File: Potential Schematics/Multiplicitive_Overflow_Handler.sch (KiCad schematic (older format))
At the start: 7 parts, among them SW1 SW_Push, U25 74LS04, U26 74LS08, U28 74LS08

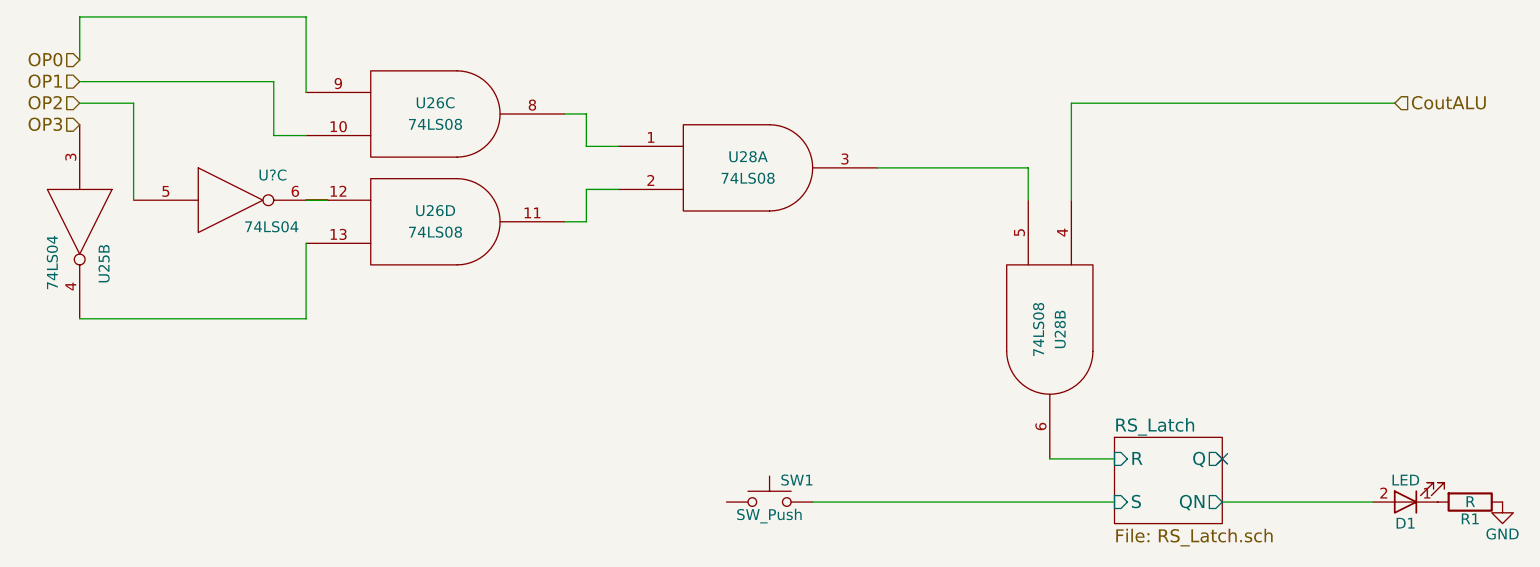
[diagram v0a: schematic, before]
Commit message: Updated overview of Schematic
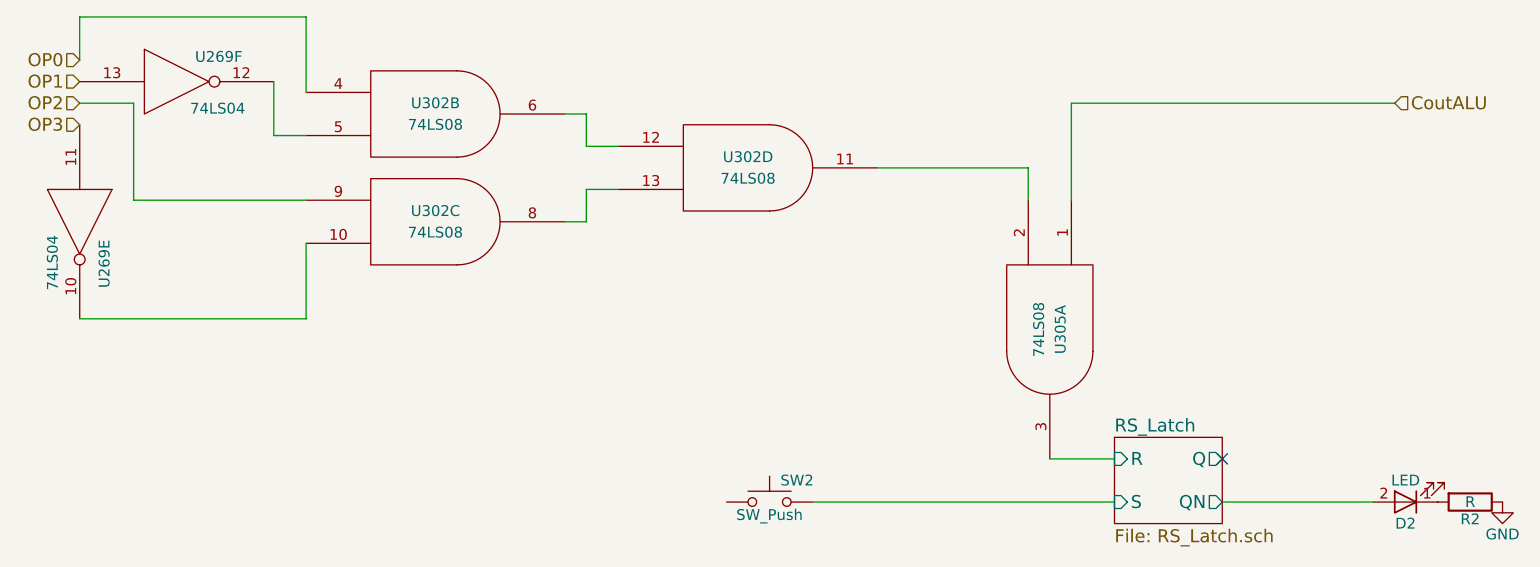
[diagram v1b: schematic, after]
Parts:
- removed U?: 74LS04, Daniel_Kopp:DIP-14_300_ELL, symbol 4-bit_processor-rescue:74LS04
- added unit 6 of U25
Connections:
- net CoutALU: now also U28.1; no longer U28.4
- net GND: now also U25.7 (GND)
- net OP0: now also U26.4; no longer U26.9
- net OP1: now also U25.13; no longer U26.10
- net OP2: now also U26.9
- net OP3: now also U25.11; no longer U25.3
- net RS_Latch/R: now also U28.3; no longer U28.6
- net VCC: now also U25.14 (VCC)
- new net: U25.10, U26.10
- new net: U26.8, U28.13
- new net: U25.12, U26.5
- new net: U26.6, U28.12
- new net: U28.11, U28.2
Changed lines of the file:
@@
 $Descr A4 11693 8268
 encoding utf-8
-Sheet 21 902
+Sheet 466 902
 Title "Integer Overflow Handler"
 Date "2018-09-14"
@@
 $Comp
 L 4-bit_processor-rescue:74LS08 U26
-U 4 1 5B9D62F2
+U 3 1 5B9D62F2
 P 3600 3400
 AR Path="/5B9D167A/5B9D5FC6/5B9D62F2" Ref="U26"  Part="4"
 AR Path="/5B9D167A/5BB0D9CD/5B9D62F2" Ref="U302"  Part="3"
-F 0 "U26" H 3600 3450 50  0000 C CNN
+F 0 "U302" H 3600 3450 50  0000 C CNN
 F 1 "74LS08" H 3600 3350 50  0000 C CNN
 F 2 "Daniel_Kopp:DIP-14_300_ELL" H 3600 3400 50  0001 C CNN
 F 3 "" H 3600 3400 50  0001 C CNN
-	4    3600 3400
+	3    3600 3400
 	1    0    0    -1
 $EndComp
 $Comp
 L 4-bit_processor-rescue:74LS08 U26
-U 3 1 5B9D634D
+U 2 1 5B9D634D
 P 3600 2900
 AR Path="/5B9D167A/5B9D5FC6/5B9D634D" Ref="U26"  Part="3"
 AR Path="/5B9D167A/5BB0D9CD/5B9D634D" Ref="U302"  Part="2"
-F 0 "U26" H 3600 2950 50  0000 C CNN
+F 0 "U302" H 3600 2950 50  0000 C CNN
 F 1 "74LS08" H 3600 2850 50  0000 C CNN
 F 2 "Daniel_Kopp:DIP-14_300_ELL" H 3600 2900 50  0001 C CNN
 F 3 "" H 3600 2900 50  0001 C CNN
-	3    3600 2900
+	2    3600 2900
 	1    0    0    -1
 $EndComp
 $Comp
 L 4-bit_processor-rescue:74LS08 U28
-U 2 1 5B9D6375
+U 1 1 5B9D6375
 P 6450 3900
 AR Path="/5B9D167A/5B9D5FC6/5B9D6375" Ref="U28"  Part="2"
 AR Path="/5B9D167A/5BB0D9CD/5B9D6375" Ref="U305"  Part="1"
-F 0 "U28" H 6450 3950 50  0000 C CNN
+F 0 "U305" H 6450 3950 50  0000 C CNN
 F 1 "74LS08" H 6450 3850 50  0000 C CNN
 F 2 "Daniel_Kopp:DIP-14_300_ELL" H 6450 3900 50  0001 C CNN
 F 3 "" H 6450 3900 50  0001 C CNN
-	2    6450 3900
+	1    6450 3900
 	0    1    1    0
 $EndComp
 $Comp
 L 4-bit_processor-rescue:74LS08 U28
-U 1 1 5B9D643C
+U 4 1 5B9D643C
 P 5050 3150
 AR Path="/5B9D167A/5B9D5FC6/5B9D643C" Ref="U28"  Part="1"
 AR Path="/5B9D167A/5BB0D9CD/5B9D643C" Ref="U302"  Part="4"
-F 0 "U28" H 5050 3200 50  0000 C CNN
+F 0 "U302" H 5050 3200 50  0000 C CNN
 F 1 "74LS08" H 5050 3100 50  0000 C CNN
 F 2 "Daniel_Kopp:DIP-14_300_ELL" H 5050 3150 50  0001 C CNN
 F 3 "" H 5050 3150 50  0001 C CNN
-	1    5050 3150
+	4    5050 3150
 	1    0    0    -1
 $EndComp
@@
 Wire Wire Line
 	2200 2850 2200 3300
+Wire Wire Line
+	2200 3300 3000 3300
 $Comp
 L 4-bit_processor-rescue:74LS04 U25
-U 2 1 5B9D6565
+U 5 1 5B9D6565
 P 1950 3400
 AR Path="/5B9D167A/5B9D5FC6/5B9D6565" Ref="U25"  Part="2"
 AR Path="/5B9D167A/5BB0D9CD/5B9D6565" Ref="U269"  Part="5"
-F 0 "U25" H 2145 3515 50  0000 C CNN
+F 0 "U269" H 2145 3515 50  0000 C CNN
 F 1 "74LS04" H 2140 3275 50  0000 C CNN
 F 2 "Daniel_Kopp:DIP-14_300_ELL" H 1950 3400 50  0001 C CNN
 F 3 "" H 1950 3400 50  0001 C CNN
-	2    1950 3400
+	5    1950 3400
 	0    1    1    0
 $EndComp
@@
 AR Path="/5B9D167A/5B9D5FC6/5B9D6685" Ref="D1"  Part="1"
 AR Path="/5B9D167A/5BB0D9CD/5B9D6685" Ref="D2"  Part="1"
-F 0 "D1" H 8100 4800 50  0000 C CNN
+F 0 "D2" H 8100 4800 50  0000 C CNN
 F 1 "LED" H 8100 4600 50  0000 C CNN
 F 2 "LEDs:LED_D1.8mm_W1.8mm_H2.4mm_Horizontal_O3.81mm_Z4.9mm" H 8100 4700 50  0001 C CNN
@@
 AR Path="/5B9D167A/5B9D5FC6/5B9D6786" Ref="R1"  Part="1"
 AR Path="/5B9D167A/5BB0D9CD/5B9D6786" Ref="R2"  Part="1"
-F 0 "R1" V 8480 4700 50  0000 C CNN
+F 0 "R2" V 8480 4700 50  0000 C CNN
 F 1 "R" V 8400 4700 50  0000 C CNN
 F 2 "Resistors_THT:R_Axial_DIN0922_L20.0mm_D9.0mm_P30.48mm_Horizontal" V 8330 4700 50  0001 C CNN
@@
 AR Path="/5B9D167A/5B9D5FC6/5B9D67B7" Ref="#PWR01"  Part="1"
 AR Path="/5B9D167A/5BB0D9CD/5B9D67B7" Ref="#PWR02"  Part="1"
-F 0 "#PWR01" H 8550 4450 50  0001 C CNN
+F 0 "#PWR02" H 8550 4450 50  0001 C CNN
 F 1 "GND" H 8550 4550 50  0000 C CNN
 F 2 "" H 8550 4700 50  0001 C CNN
@@
 AR Path="/5B9D167A/5B9D5FC6/5B9D789D" Ref="SW1"  Part="1"
 AR Path="/5B9D167A/5BB0D9CD/5B9D789D" Ref="SW2"  Part="1"
-F 0 "SW1" H 5200 4800 50  0000 L CNN
+F 0 "SW2" H 5200 4800 50  0000 L CNN
 F 1 "SW_Push" H 5150 4640 50  0000 C CNN
 F 2 "Buttons_Switches_THT:SW_DIP_x2_W7.62mm_Slide_LowProfile" H 5150 4900 50  0001 C CNN
@@
 	7250 4700 7950 4700
 NoConn ~ 7250 4500
+$Comp
+L 4-bit_processor-rescue:74LS04 U25
+U 6 1 5B9D652D
+P 2400 2750
+AR Path="/5B9D167A/5B9D5FC6/5B9D652D" Ref="U25"  Part="3"
+AR Path="/5B9D167A/5BB0D9CD/5B9D652D" Ref="U269"  Part="6"
+F 0 "U269" H 2595 2865 50  0000 C CNN
+F 1 "74LS04" H 2590 2625 50  0000 C CNN
+F 2 "Daniel_Kopp:DIP-14_300_ELL" H 2400 2750 50  0001 C CNN
+F 3 "" H 2400 2750 50  0001 C CNN
+	6    2400 2750
+	1    0    0    -1
+$EndComp
 Wire Wire Line
 	1950 2450 3000 2450
-$Comp
-L 4-bit_processor-rescue:74LS04 U?
-U 3 1 5BCC46E6
-P 2650 3300
-AR Path="/5B9D167A/5B9D5FC6/5BCC46E6" Ref="U?"  Part="3"
-AR Path="/5B9D167A/5BB0D9CD/5BCC46E6" Ref="U?"  Part="6"
-F 0 "U?" H 2845 3415 50  0000 C CNN
-F 1 "74LS04" H 2840 3175 50  0000 C CNN
-F 2 "Daniel_Kopp:DIP-14_300_ELL" H 2650 3300 50  0001 C CNN
-F 3 "" H 2650 3300 50  0001 C CNN
-	3    2650 3300
-	1    0    0    -1
-$EndComp
-Wire Wire Line
-	3000 3300 3100 3300
-Wire Wire Line
-	1950 2750 2850 2750
 $EndSCHEMATC
